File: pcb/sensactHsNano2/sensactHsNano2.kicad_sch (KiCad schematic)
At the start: 64 parts, among them J1 PROG, J2 SensactBusConnector, J3 CAN+24V, J5 Audio, J6 Conn_01x03, J8 Conn_01x10, SW1 TERM ON, SW2 Prog, SW3 Reset, SW4 PROG_PWR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

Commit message: Sicherung
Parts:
- added U?: MAX3485, symbol Interface_UART:MAX3485

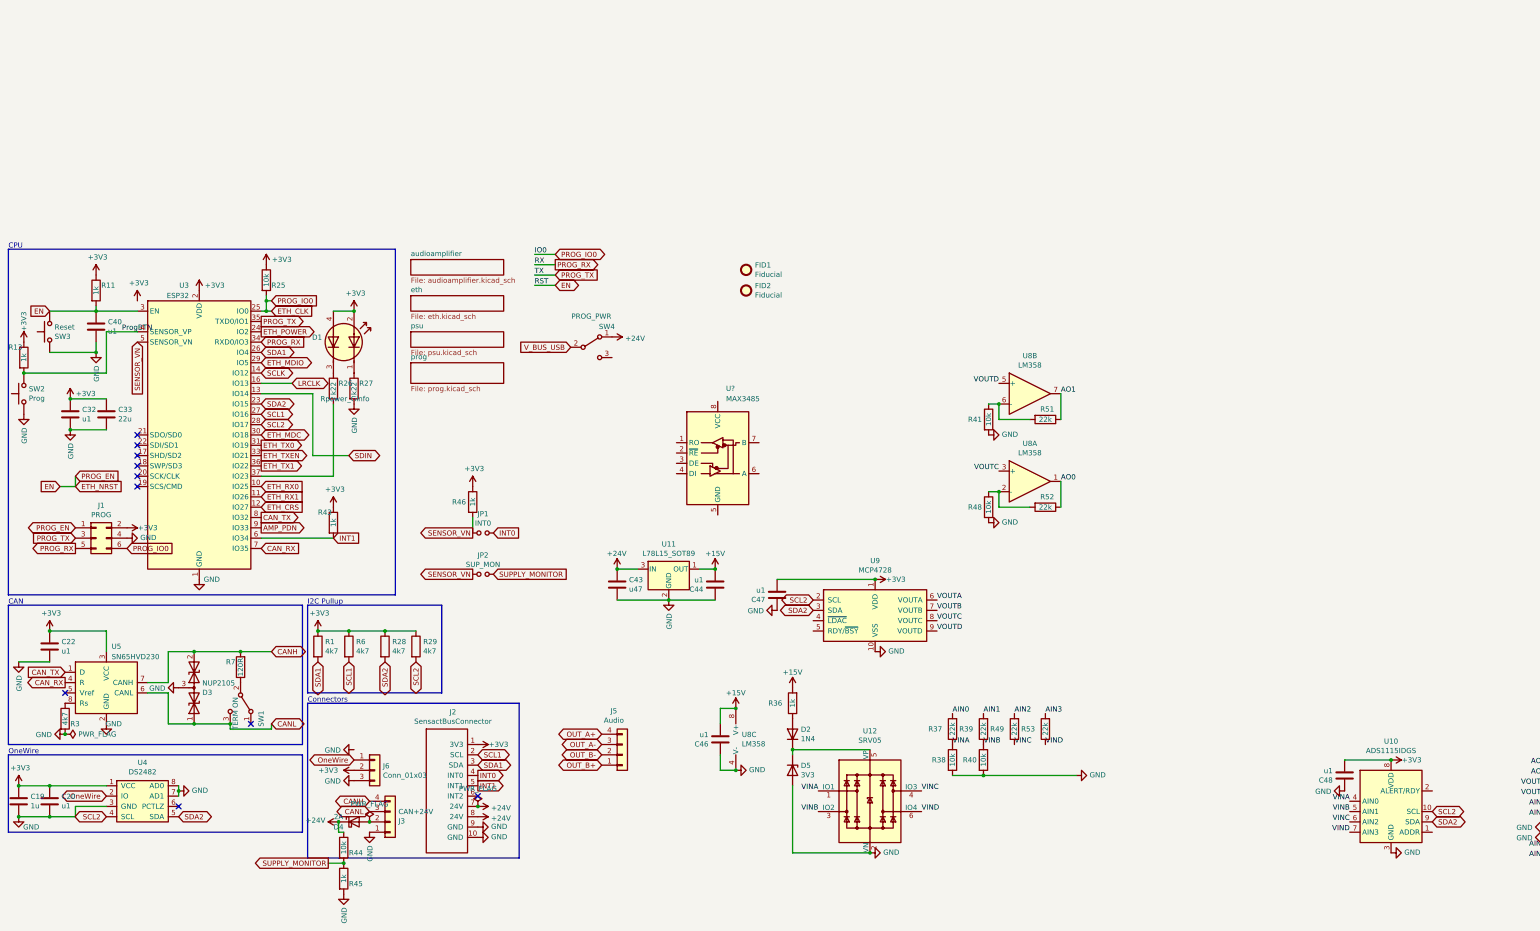
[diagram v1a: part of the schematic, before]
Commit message: DIn-schiene-seitenwand + sensactHsNano2
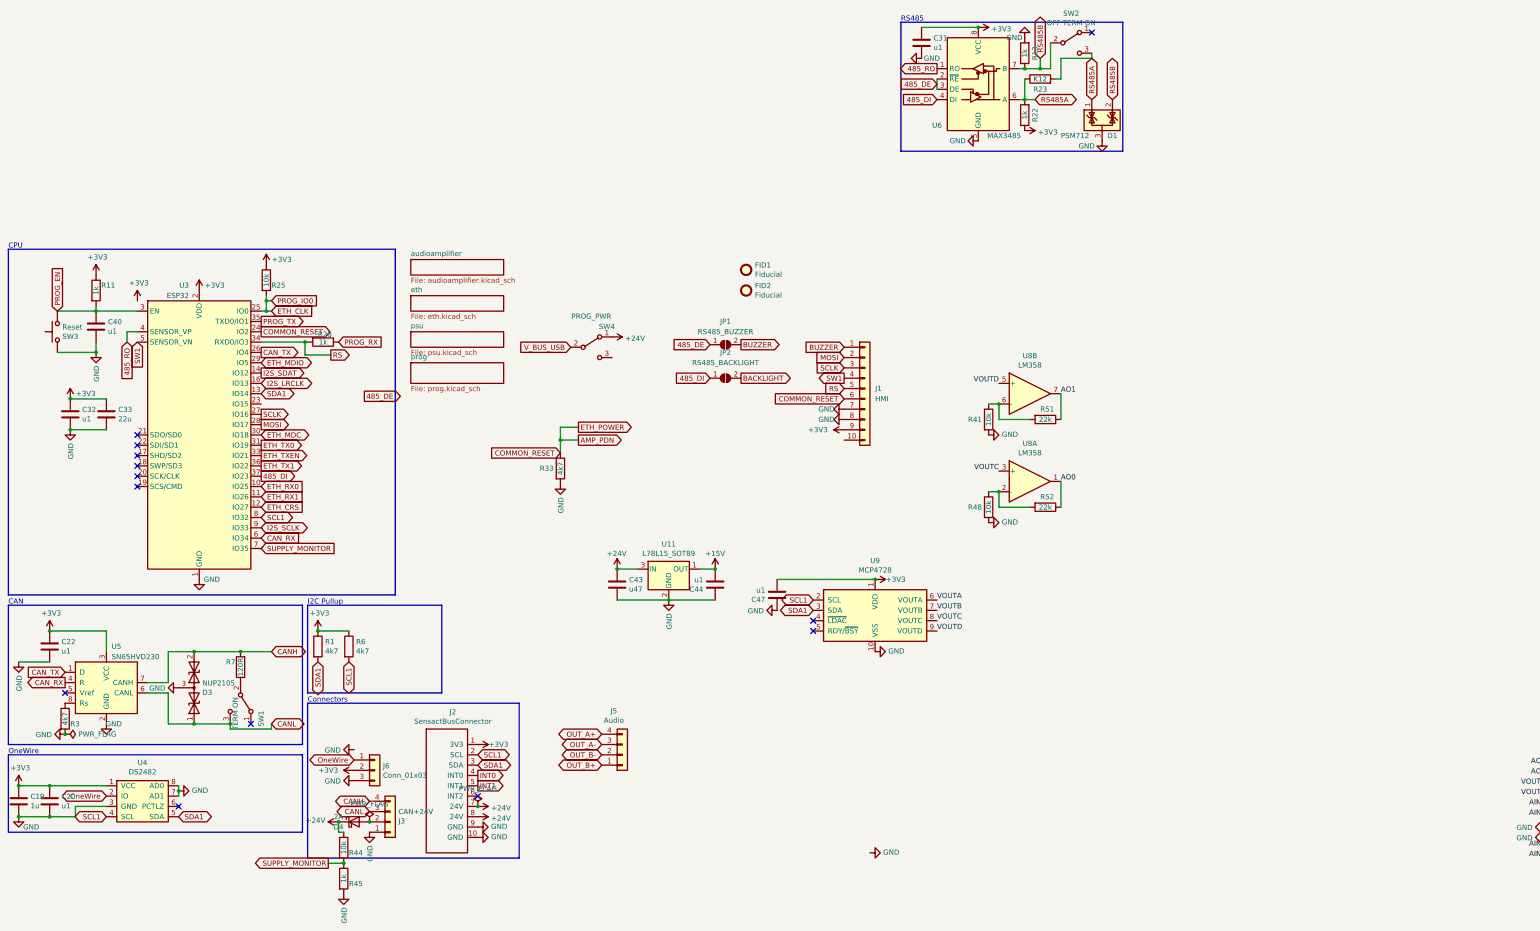
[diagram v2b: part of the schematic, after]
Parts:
- removed C46, C48: u1, Capacitor_SMD:C_0603_1608Metric, symbol Device:C
- removed D1: Rpower_Ginfo, liebler_SEMICONDUCTORS:Dialight-5530123F-0, symbol Device:LED_Dual_CACA
- removed D2: 1N4, Diode_SMD:D_SOD-123, symbol Device:D
- removed D5: 3V3, Diode_SMD:D_MiniMELF, symbol Device:D_Zener
- removed J1: PROG, liebler_CONN:IDC_2x03_P1.27mm_Vertical, symbol Connector_Generic:Conn_02x03_Odd_Even
- removed JP1: INT0, Jumper:SolderJumper-2_P1.3mm_Open_RoundedPad1.0x1.5mm, symbol Device:Jumper_NO_Small
- removed JP2: SUP_MON, Jumper:SolderJumper-2_P1.3mm_Open_RoundedPad1.0x1.5mm, symbol Device:Jumper_NO_Small
- removed R26, R27: k22, Resistor_SMD:R_0805_2012Metric_Pad1.20x1.40mm_HandSolder, symbol Device:R
- removed R29: 4k7, Resistor_SMD:R_0603_1608Metric, symbol Device:R
- removed R36: 1k, Resistor_SMD:R_0603_1608Metric, symbol Device:R
- removed R37, R39, R49, R53: 22k, Resistor_SMD:R_0603_1608Metric, symbol Device:R
- removed R38, R40: 10k, Resistor_SMD:R_0603_1608Metric, symbol Device:R
- removed R43, R46: 1k, Resistor_SMD:R_0805_2012Metric_Pad1.20x1.40mm_HandSolder, symbol Device:R
- removed SW2: Prog, Button_Switch_THT:SW_Tactile_SPST_Angled_PTS645Vx58-2LFS, symbol Switch:SW_Push
- removed U10: ADS1115IDGS, Package_SO:TSSOP-10_3x3mm_P0.5mm, symbol Analog_ADC:ADS1115IDGS
- removed U12: SRV05, Package_TO_SOT_SMD:SOT-23-6, symbol Power_Protection:SRV05-4
- removed unit 3 of U8
- removed U?: MAX3485, symbol Interface_UART:MAX3485
- added C31: u1, Capacitor_SMD:C_0603_1608Metric, symbol Device:C
- added D1: PSM712, Package_TO_SOT_SMD:SOT-23, symbol Power_Protection:NUP2105L
- added J1: HMI, Connector_FFC-FPC:Hirose_FH12-10S-0.5SH_1x10-1MP_P0.50mm_Horizontal, symbol Connector_Generic:Conn_01x10
- added JP1: RS485_BUZZER, symbol Jumper:SolderJumper_2_Open
- added JP2: RS485_BACKLIGHT, symbol Jumper:SolderJumper_2_Open
- added R22: 1k, Resistor_SMD:R_0603_1608Metric, symbol Device:R
- added R23: K12, Resistor_SMD:R_0603_1608Metric, symbol Device:R
- added R33: 4k7, Resistor_SMD:R_0402_1005Metric, symbol Device:R
- added SW2: OFF TERM ON, liebler_MECH:Switch_SS12D00, symbol Switch:SW_SPDT
- added U6: MAX3485, Package_SO:SOIC-8_3.9x4.9mm_P1.27mm, symbol Interface_UART:MAX3485
- C22, C32: footprint Capacitor_SMD:C_0603_1608Metric -> Capacitor_SMD:C_0402_1005Metric
- C40: footprint Capacitor_SMD:C_0805_2012Metric_Pad1.18x1.45mm_HandSolder -> Capacitor_SMD:C_0402_1005Metric
- R11, R3, R44, R45: footprint Resistor_SMD:R_0805_2012Metric_Pad1.20x1.40mm_HandSolder -> Resistor_SMD:R_0402_1005Metric
- R13: footprint Resistor_SMD:R_0805_2012Metric_Pad1.20x1.40mm_HandSolder -> Resistor_SMD:R_0603_1608Metric
- R25: footprint Resistor_SMD:R_0603_1608Metric -> Resistor_SMD:R_0402_1005Metric
- R28: value 4k7 -> 1k; footprint Resistor_SMD:R_0603_1608Metric -> Resistor_SMD:R_0402_1005Metric
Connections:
- net ETH_POWER is gone; now on net AMP_PDN: U3.24 (IO2)
- net SDIN is gone; now on net SDA1: U3.13 (IO14)
- net +3V3: now also C31.2, J1.9 (Pin_9), R22.1, U6.8 (VCC); no longer R13.1, R28.1
- net AMP_PDN: now also J1.6 (Pin_6), R33.1; no longer U3.9 (IO33)
- net CAN_RX: now also U3.6 (IO34); no longer U3.7 (IO35)
- net CAN_TX: now also U3.26 (IO4); no longer U3.8 (IO32)
- net GND: now also R13.2, C31.1, D1.3 (A), J1.7 (Pin_7), J1.8 (Pin_8), R33.2, U6.5 (GND)
- net INT1: no longer U3.6 (IO34)
- net PROG_RX: now also R28.1; no longer U3.34 (RXD0/IO3)
- net SCL1: now also U3.8 (IO32), U4.4 (SCL), U9.2 (SCL); no longer U3.27 (IO16)
- net SCLK: now also U3.27 (IO16), J1.3 (Pin_3); no longer U3.14 (IO12)
- net SDA1: now also U4.5 (SDA), U9.3 (SDA); no longer U3.26 (IO4)
- net SUPPLY_MONITOR: now also U3.7 (IO35)
- net 485_DI: now reaches U3.37 (IO23)
- net 485_DI: now also JP2.1 (A), U6.4 (DI)
- net EN renamed PROG_EN
- net LRCLK renamed I2S_LRCLK
- net ProgBTN renamed 485_RO
- net 485_RO: now also U6.1 (RO); no longer R13.2
- removed net SCL2: U3.28 (IO17), U4.4 (SCL), U9.2 (SCL)
- removed net SDA2: R28.2, U3.23 (IO15), U4.5 (SDA), U9.3 (SDA)
- net SENSOR_VN renamed SW1
- net SW1: now also J1.4 (Pin_4)
- new net: R23.2, SW2.3 (C)
- new net 485_DE: JP1.1 (A), U6.2 (~{RE}), U6.3 (DE)
- new net BACKLIGHT: JP2.2 (B)
- new net BUZZER: J1.1 (Pin_1), JP1.2 (B)
- new net I2S_SCLK: U3.9 (IO33)
- new net I2S_SDAT: U3.14 (IO12)
- new net MOSI: J1.2 (Pin_2), U3.28 (IO17)
- new net RS: J1.5 (Pin_5), R28.2, U3.34 (RXD0/IO3)
- new net RS485A: D1.1 (K), R22.2, R23.1, U6.6 (A)
- new net RS485B: D1.2 (K), R13.1, SW2.2 (B), U6.7 (B)
- no-connect marks 10 -> 13
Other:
- note added: "RS485"
- moved on the sheet: SW3

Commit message: sensactNanoHS2
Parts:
- removed D4: 2A, Diode_SMD:D_SMB_Handsoldering, symbol Device:D_Schottky
- removed FID1, FID2: Fiducial, Fiducial:Fiducial_1.5mm_Mask3mm, symbol Mechanical:Fiducial
- added C46: u1, Capacitor_SMD:C_0402_1005Metric, symbol Device:C
- added D2: 2A, Diode_SMD:D_SMB_Handsoldering, symbol Device:D_Schottky
- added J9: 24V, Connector_Phoenix_MC:PhoenixContact_MC_1,5_2-G-3.81_1x02_P3.81mm_Horizontal, symbol Connector_Generic:Conn_01x02
- added unit 3 of U8
- C19, C20, C31, C44, C47: footprint Capacitor_SMD:C_0603_1608Metric -> Capacitor_SMD:C_0402_1005Metric
- D1: footprint Package_TO_SOT_SMD:SOT-23 -> Package_TO_SOT_SMD:SOT-23_Handsoldering
- J3: value CAN+24V -> CAN+485
- R23: footprint Resistor_SMD:R_0603_1608Metric -> Resistor_SMD:R_0805_2012Metric_Pad1.20x1.40mm_HandSolder
- R41, R48, R51, R52: footprint Resistor_SMD:R_0603_1608Metric -> Resistor_SMD:R_0402_1005Metric
- SW2: footprint liebler_MECH:Switch_SS12D00 -> liebler_MECH:SW_SPDT_PCM12_handsolder
- SW3: footprint Button_Switch_THT:SW_Tactile_SPST_Angled_PTS645Vx58-2LFS -> liebler_MECH:Button_2x4x3,5_handsolder
- U11: footprint Package_TO_SOT_SMD:SOT-89-3 -> Package_TO_SOT_SMD:SOT-89-3_Handsoldering
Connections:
- net +15V: now also C46.2, U8.8 (V+)
- net +24V: now also D2.1 (K)
- net 485_DE: now also U3.23 (IO15)
- net CAN_TX: now also U3.27 (IO16); no longer U3.26 (IO4)
- net GND: now also SW3.1, C46.1, J9.2 (Pin_2), U8.4 (V-); no longer J3.1 (Pin_1), SW3.2
- net MOSI: now also U3.26 (IO4); no longer U3.28 (IO17)
- net PROG_EN: now also SW3.2; no longer SW3.1
- net RS485A: now also J3.1 (Pin_1)
- net RS485B: now also J3.2 (Pin_2)
- net SCLK: now also U3.28 (IO17); no longer U3.27 (IO16)
- net VOUTA: now also U8.3 (+); no longer J8.4 (Pin_4)
- net VOUTB: now also U8.5 (+); no longer J8.3 (Pin_3)
- net VOUTC: now also J8.4 (Pin_4); no longer U8.3 (+)
- net VOUTD: now also J8.3 (Pin_3); no longer U8.5 (+)
- net V_BUS_USB renamed +5P
- new net: D2.2 (A), J9.1 (Pin_1)
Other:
- moved on the sheet: J8, R44, R45

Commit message: Improved sensactNano2
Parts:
- JP1, JP2: footprint (none) -> Jumper:SolderJumper-2_P1.3mm_Open_RoundedPad1.0x1.5mm
- R1, R6: footprint Resistor_SMD:R_0603_1608Metric -> Resistor_SMD:R_0402_1005Metric
- R23: footprint Resistor_SMD:R_0805_2012Metric_Pad1.20x1.40mm_HandSolder -> Resistor_SMD:R_1206_3216Metric_Pad1.30x1.75mm_HandSolder
- R7: value 120R -> K12
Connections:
- net AIN0 is gone; now on net +24V: J8.9 (Pin_9)
- net AIN1 is gone; now on net +24V: J8.10 (Pin_10)
- net AIN2 is gone; now on net +3V3: J8.5 (Pin_5)
- net AIN3 is gone; now on net +3V3: J8.6 (Pin_6)
- net +24V: now also SW4.3 (C); no longer SW4.1 (A)
- net BACKLIGHT: now also J1.10 (Pin_10)
- net CANH: now also J3.1 (Pin_1); no longer J3.4 (Pin_4)
- net CANL: now also J3.2 (Pin_2), SW1.2 (B); no longer J3.3 (Pin_3)
- net CAN_TX: now also U3.28 (IO17); no longer U3.27 (IO16)
- net ETH_MDC: now also U3.29 (IO5); no longer U3.30 (IO18)
- net ETH_MDIO: now also U3.30 (IO18); no longer U3.29 (IO5)
- net I2S_SCLK: now also U3.14 (IO12); no longer U3.9 (IO33)
- net I2S_SDAT: now also U3.9 (IO33); no longer U3.14 (IO12)
- net RS485A: now also J3.4 (Pin_4); no longer J3.1 (Pin_1)
- net RS485B: now also J3.3 (Pin_3), SW2.3 (C); no longer J3.2 (Pin_2)
- net SCLK: now also U3.27 (IO16); no longer U3.28 (IO17)
- net at R7.1: now also SW1.1 (A); no longer SW1.2 (B)
- net at R23.2: now also SW2.1 (A); no longer SW2.3 (C)
- no-connect marks 13 -> 11
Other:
- note added: "PD!"
- note added: "PU!"
- note added: "PU?"
- moved on the sheet: SW1

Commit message: Various
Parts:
- added C48: u1, Capacitor_SMD:C_0805_2012Metric_Pad1.18x1.45mm_HandSolder, symbol Device:C
- added JP3: SolderJumper_2_Open, Jumper:SolderJumper-2_P1.3mm_Open_RoundedPad1.0x1.5mm, symbol Jumper:SolderJumper_2_Open
- added R2: r1, Resistor_SMD:R_1206_3216Metric_Pad1.30x1.75mm_HandSolder, symbol Device:R
- added U10: INA219AxD, liebler_SEMICONDUCTORS:SOIC-8_3.9x4.9mm_Pitch1.27mm_handsolder, symbol Analog_ADC:INA219AxD
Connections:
- net +24V: now also JP3.2 (B), R2.2, U10.7 (IN-); no longer D2.1 (K)
- net +3V3: now also C48.2, U10.5 (VS)
- net GND: now also C48.1, U10.1 (A1), U10.2 (A0), U10.6 (GND)
- net SCL1: now also U10.4 (SCL)
- net SDA1: now also U10.3 (SDA)
- new net: D2.1 (K), JP3.1 (A), R2.1, U10.8 (IN+)
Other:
- note added: "I2C-Adressen MCP4728 0b 1100000 INA219 0b 100xxxx DS2482 0b 00110xx TAS5805 0b 01011xx PCA9685 0b 1110000 All Call 0b 0000011 SW Reset 0b 1xxxxxx(der erste Geht nicht wg INA219) PCA9555 0b 0100xxx"
- moved on the sheet: D2, J9

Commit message: Various
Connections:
- net CAN_RX: now also U3.5 (SENSOR_VN); no longer U3.6 (IO34)
- net SW1: now also U3.6 (IO34); no longer U3.5 (SENSOR_VN)
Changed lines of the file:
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@@
     )
   )
-  (global_label "CAN_RX" (shape input) (at 74.93 86.36 0) (fields_autoplaced)
-    (effects (font (size 1.27 1.27)) (justify left))
-    (property "Intersheet References" "${INTERSHEET_REFS}" (id 0) (at 0 -2.54 0)
+  (global_label "CAN_RX" (shape input) (at 44.45 38.1 270) (fields_autoplaced)
+    (effects (font (size 1.27 1.27)) (justify right))
+    (property "Intersheet References" "${INTERSHEET_REFS}" (id 0) (at 133.35 -36.83 0)
       (effects (font (size 1.27 1.27)) hide)
     )
@@
     )
   )
-  (global_label "SW1" (shape input) (at 44.45 38.1 270) (fields_autoplaced)
-    (effects (font (size 1.27 1.27)) (justify right))
-    (property "Intersheet References" "${INTERSHEET_REFS}" (id 0) (at 44.3706 44.2947 90)
-      (effects (font (size 1.27 1.27)) (justify right) hide)
+  (global_label "SW1" (shape input) (at 74.93 86.36 0) (fields_autoplaced)
+    (effects (font (size 1.27 1.27)) (justify left))
+    (property "Intersheet References" "${INTERSHEET_REFS}" (id 0) (at 81.1247 86.4394 0)
+      (effects (font (size 1.27 1.27)) (justify left) hide)
     )
   )
@@
       (reference "#PWR012") (unit 1) (value "GND") (footprint "")
     )
-    (path "/00000000-0000-0000-0000-000060e30b7a/00000000-0000-0000-0000-00005e10cb5e"
+    (path "/00000000-0000-0000-0000-00006181a2e2/3a9196e9-edcd-4f47-bb3f-07f82e25dbdc"
       (reference "#PWR013") (unit 1) (value "GND") (footprint "")
     )
@@
       (reference "#PWR014") (unit 1) (value "+3V3") (footprint "")
     )
-    (path "/00000000-0000-0000-0000-000060e30b7a/00000000-0000-0000-0000-00005e0b73e9"
-      (reference "#PWR015") (unit 1) (value "GND") (footprint "")
-    )
     (path "/00000000-0000-0000-0000-000060e30b7a/00000000-0000-0000-0000-00005e0dad05"
       (reference "#PWR016") (unit 1) (value "GND") (footprint "")
@@
       (reference "#PWR025") (unit 1) (value "GND") (footprint "")
     )
-    (path "/00000000-0000-0000-0000-000060e30b7a/00000000-0000-0000-0000-00005e10d619"
-      (reference "#PWR026") (unit 1) (value "GND") (footprint "")
-    )
     (path "/00000000-0000-0000-0000-000060e5a575"
       (reference "#PWR027") (unit 1) (value "+3V3") (footprint "")
@@
       (reference "#PWR0151") (unit 1) (value "+3V3") (footprint "")
     )
+    (path "/00000000-0000-0000-0000-000060e30b7a/e7cb7bc1-2d67-4af7-b28d-d561be0de79a"
+      (reference "#PWR0152") (unit 1) (value "GND") (footprint "")
+    )
     (path "/00000000-0000-0000-0000-00005f9c3c99/00000000-0000-0000-0000-00005f9dd337"
       (reference "C1") (unit 1) (value "470u") (footprint "Capacitor_THT:CP_Radial_D10.0mm_P3.50mm")
@@
     )
     (path "/00000000-0000-0000-0000-000060e30b7a/00000000-0000-0000-0000-00005e109cd1"
-      (reference "C21") (unit 1) (value "u1") (footprint "Capacitor_SMD:C_0805_2012Metric_Pad1.18x1.45mm_HandSolder")
+      (reference "C21") (unit 1) (value "u1") (footprint "Capacitor_SMD:C_0402_1005Metric")
     )
     (path "/00000000-0000-0000-0000-00005fa43ad6"
@@
     )
     (path "/00000000-0000-0000-0000-00006181a2e2/eb914753-4ad8-44fc-93fd-14f530d0ab5b"
-      (reference "J7") (unit 1) (value "PROG") (footprint "liebler_CONN:USB_C_Receptacle_HRO_TYPE-C-31-M-12_IMPROVED")
+      (reference "J7") (unit 1) (value "PROG") (footprint "liebler_CONN:USB_C_Receptacle_HRO_TYPE-C-31-M-12_smaller")
     )
     (path "/00000000-0000-0000-0000-000061938435"
@@
       (reference "NT1") (unit 1) (value "Net-Tie_2") (footprint "NetTie:NetTie-2_SMD_Pad2.0mm")
     )
+    (path "/00000000-0000-0000-0000-000060e30b7a/c83ee589-2a8a-4166-bee2-d2f600b8d91e"
+      (reference "NT2") (unit 1) (value "NetTie_2") (footprint "NetTie:NetTie-2_SMD_Pad0.5mm")
+    )
     (path "/00000000-0000-0000-0000-00006181a2e2/dd64bd92-873a-41e2-947c-df9be8b62d94"
-      (reference "Q1") (unit 1) (value "BC817") (footprint "Package_TO_SOT_SMD:SOT-23")
+      (reference "Q1") (unit 1) (value "BC817") (footprint "liebler_SEMICONDUCTORS:SOT-23_smaller")
     )
     (path "/00000000-0000-0000-0000-00006181a2e2/32659d89-6784-4859-9fd1-5b6349b2ee2a"
-      (reference "Q2") (unit 1) (value "BC817") (footprint "Package_TO_SOT_SMD:SOT-23")
+      (reference "Q2") (unit 1) (value "BC817") (footprint "liebler_SEMICONDUCTORS:SOT-23_smaller")
     )
     (path "/00000000-0000-0000-0000-00005fa49518"
@@
     )
     (path "/00000000-0000-0000-0000-00005f9c3c99/00000000-0000-0000-0000-000061306266"
-      (reference "U1") (unit 1) (value "TAS5805M") (footprint "liebler_SEMICONDUCTORS:TSSOP-28_4.4x9.7mm_Pitch0.65mm_pad_handsolder")
+      (reference "U1") (unit 1) (value "TAS5805M") (footprint "Package_SO:HTSSOP-28-1EP_4.4x9.7mm_P0.65mm_EP2.85x5.4mm_ThermalVias")
     )
     (path "/00000000-0000-0000-0000-000060e30b7a/00000000-0000-0000-0000-00006124e6ff"
@@
       (reference "U11") (unit 1) (value "L78L15_SOT89") (footprint "Package_TO_SOT_SMD:SOT-89-3_Handsoldering")
     )
-    (path "/00000000-0000-0000-0000-00006181a2e2/f00e656c-e83a-4766-909c-2e0d3eea4f0e"
-      (reference "U13") (unit 1) (value "CH340C") (footprint "Package_SO:SOIC-16_3.9x9.9mm_P1.27mm")
+    (path "/00000000-0000-0000-0000-00006181a2e2/e46ba44c-f9ee-428c-a18c-f36ebf366e7e"
+      (reference "U12") (unit 1) (value "CH340K") (footprint "liebler_SEMICONDUCTORS:SSOP-10_3.9x4.9mm_P1.00mm_EP")
     )
     (path "/00000000-0000-0000-0000-000060e30b7a/00000000-0000-0000-0000-00005e0b1bef"
-      (reference "X1") (unit 1) (value "50MHz") (footprint "Oscillator:Oscillator_SMD_EuroQuartz_XO32-4Pin_3.2x2.5mm_HandSoldering")
-    )
-  )
+      (reference "X1") (unit 1) (value "50MHz") (footprint "Oscillator:Oscillator_SMD_SeikoEpson_SG8002CE-4Pin_3.2x2.5mm")
+    )
+  )
